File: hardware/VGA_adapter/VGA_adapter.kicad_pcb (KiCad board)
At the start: 2 copper layers, 19.2 x 25.8 mm, 38 parts, among them J1 DF12NB(3.0)-30DS-0.5V(51), J2 DF12NB(3.0)-30DS-0.5V(51), J3 FPC Cable connector 1x15, U1 TXS0102DQMR

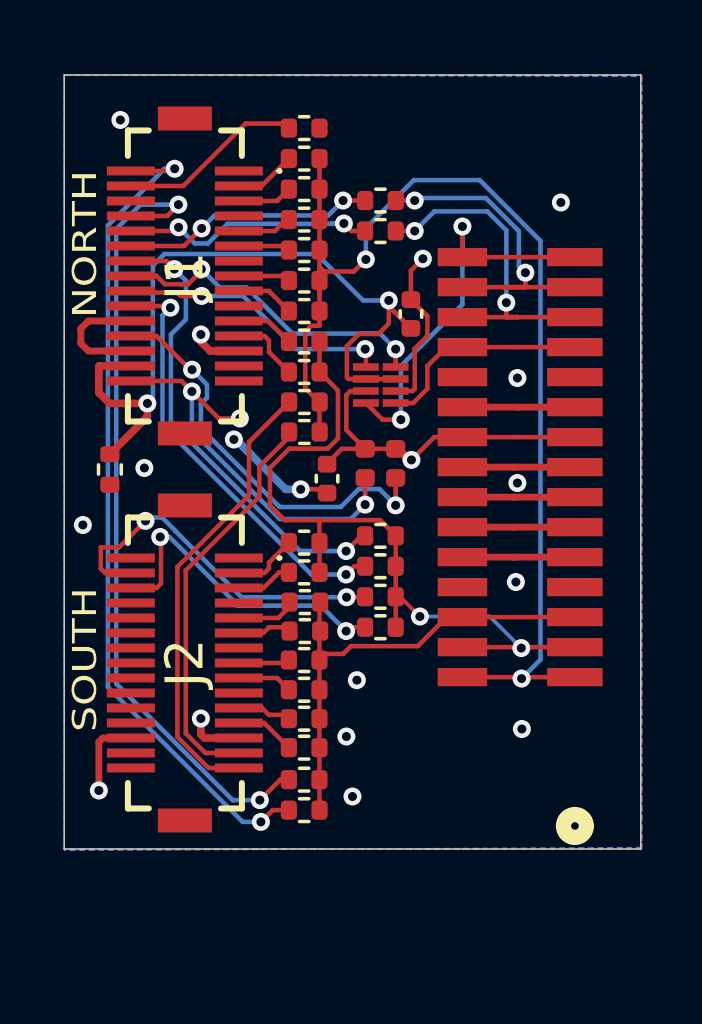
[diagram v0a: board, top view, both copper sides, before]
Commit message: Fix transitors (correct is NMOS, fast version selected). Added charge pump. Fixed level translator pinout.
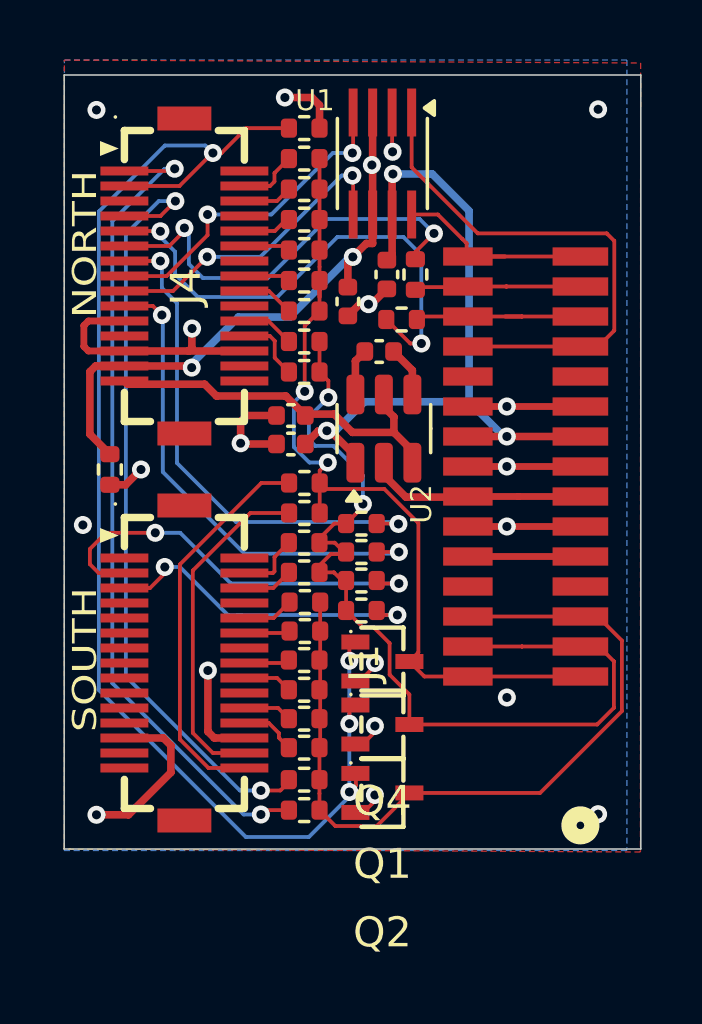
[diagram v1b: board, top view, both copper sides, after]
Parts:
- removed D1, D2: NSR05F40NXT5G, Diode_SMD:D_0402_1005Metric
- removed J2: DF12NB(3.0)-30DS-0.5V(51), Library:DF12NB3030DP05V51
- added C3: 2.2uF, Capacitor_SMD:C_0402_1005Metric, F.Cu at (153.8, 93.0)
- added C4: 2.2uF, Capacitor_SMD:C_0402_1005Metric, F.Cu at (153.8, 92.1)
- added C5: 2.2uF, Capacitor_SMD:C_0402_1005Metric, F.Cu at (156.7, 90.0)
- added J4: DF12NB(3.0)-30DS-0.5V(51), easyeda2kicad:CONN-SMD_30P-P0.50_HRS_DF12NB-3.0-30DP-0.5V, F.Cu at (150.2, 87.4)
- added Q1: NX3008NBKW,115, easyeda2kicad:SOT-323-3_L2.0-W1.3-P1.30-LS2.1-BR, F.Cu at (156.8, 102.4)
- added Q2: NX3008NBKW,115, easyeda2kicad:SOT-323-3_L2.0-W1.3-P1.30-LS2.1-BR, F.Cu at (156.8, 104.7)
- added Q4: NX3008NBKW,115, easyeda2kicad:SOT-323-3_L2.0-W1.3-P1.30-LS2.1-BR, F.Cu at (156.8, 100.3)
- added U2: HE9009M6R, Package_TO_SOT_SMD:SOT-23-6, F.Cu at (156.9, 92.5)
- C1, C2: value 0.1uF -> 2.2uF; footprint Library:C_0402_1005Metric -> Capacitor_SMD:C_0402_1005Metric
- J1: footprint Library:DF12NB3030DP05V51 -> easyeda2kicad:CONN-SMD_30P-P0.50_HRS_DF12NB-3.0-30DP-0.5V
- U1: value TXS0102DQMR -> TXS0102DCT; footprint Library:DQM8 -> Package_SO:SSOP-8_2.95x2.8mm_P0.65mm
- moved J1 12.9 mm to (150.2, 100.3), turned to -90 degrees
- moved G*** 10.5 mm to (152.5, 96.8)
- moved U1 7.38 mm to (156.8, 83.7), turned to -90 degrees
- moved C2 5.95 mm to (155.7, 88.3)
- moved G*** 4.00 mm to (150.0, 82.6), turned to 0 degrees
- moved R27 3.03 mm to (157.5, 88.9)
- moved R28 2.73 mm to (157.9, 87.4), turned to -90 degrees
- moved R8 2.70 mm to (154.2, 94.3)
- moved R9 2.70 mm to (154.2, 95.3)
- moved C1 1.54 mm to (157.0, 87.4), turned to -90 degrees
- moved R12 0.85 mm to (156.2, 98.6), turned to 0 degrees
- moved R13 0.83 mm to (156.2, 97.6), turned to 0 degrees
- moved R17 0.79 mm to (156.2, 96.7), turned to 0 degrees
- moved R16 0.75 mm to (156.2, 95.7), turned to 0 degrees
- moved J3 0.18 mm to (163.4, 100.8)
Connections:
- C1 pad 1: VCC3V3 -> V_VGA
- C2 pad 1: V_VGA -> VCC3V3
- J1 pad 10: Net-(J1-9) -> B6
- J1 pad 11: R5 -> unconnected-(J1-12-Pad11)
- J1 pad 12: Net-(J1-11) -> B7
- J1 pad 14: G1 -> unconnected-(J1-13-Pad14)
- J1 pad 15: R2 -> unconnected-(J1-16-Pad15)
- J1 pad 16: SDA -> B4
- J1 pad 17: R3 -> unconnected-(J1-18-Pad17)
- J1 pad 18: SCK -> B5
- J1 pad 2: B1 -> unconnected-(J1-1-Pad2)
- J1 pad 20: G0 -> unconnected-(J1-19-Pad20)
- J1 pad 21: G6 -> unconnected-(J1-22-Pad21)
- J1 pad 22: GND -> B2
- J1 pad 23: G7 -> unconnected-(J1-24-Pad23)
- J1 pad 24: VCCIN -> B3
- J1 pad 28: VCC3V3 -> R0
- J1 pad 3: R6 -> G4
- J1 pad 30: +3V3 -> R1
- J1 pad 4: LCD_DE -> G2
- J1 pad 5: R7 -> G5
- J1 pad 6: unconnected-(J1-5-Pad6) -> G3
- J1 pad 8: B0 -> unconnected-(J1-7-Pad8)
- J1 pad 9: R4 -> unconnected-(J1-10-Pad9)
- R27 pad 1: Net-(J1-9) -> /HSYNC_IN
- R28 pad 1: Net-(J1-11) -> /VSYNC_IN
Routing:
- net LCD_DE: track 6.19 -> 44.6 mm, vias 0 -> 4
- net /HSYNC_IN: track 0.00 -> 16.9 mm, vias 0 -> 2
- net /VSYNC_IN: track 0.00 -> 14.1 mm, vias 0 -> 2
- net VCCIN: track 13.9 -> 0.00 mm, vias 2 -> 0
- net V_VGA: track 12.5 -> 25.3 mm, vias 1 -> 3
- net GND: track 39.7 -> 51.7 mm, vias 17 -> 19
- net RED: track 39.8 -> 28.4 mm
- net BLUE: track 16.3 -> 26.9 mm
- net SDA_SHIFTED: track 7.19 -> 17.7 mm
- net Net-(J1-9): track 8.46 -> 0.00 mm, vias 2 -> 0
- net Net-(J1-11): track 8.44 -> 0.00 mm, vias 2 -> 0
- net GREEN: track 26.4 -> 32.4 mm
- net VCC3V3: track 25.9 -> 20.0 mm, vias 2 -> 3
- net SCK_SHIFTED: track 13.5 -> 7.70 mm, vias 2 -> 0
- net LCD_VSYNC: track 11.1 -> 5.49 mm, vias 2 -> 0
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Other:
- board text added: "VERSION:"
- board text added: "VGA adapter v0.11"
- board text removed: "+"
- board text removed: "-"
- board text removed: "CERN OHL-S license"
- board text removed: "VGA Adapter V0.09"

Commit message: fixed mixup of pins G5/G4 (3rd diff pair ODD) and DE/PCLK (3rd diff pair EVEN), now with correct polarity for diff pairs
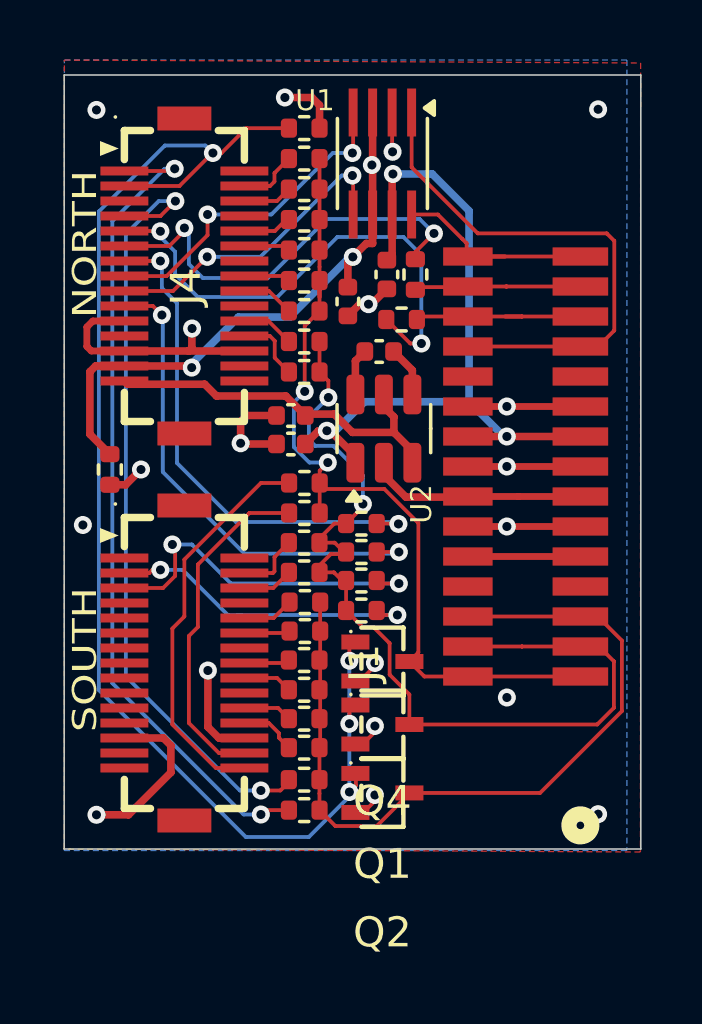
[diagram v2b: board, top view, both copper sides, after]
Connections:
- J1 pad 3: G4 -> G5
- J1 pad 5: G5 -> G4
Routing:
- net G4: track 14.0 -> 11.8 mm

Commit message: review and update manufacturing constraints (via size, etc.)
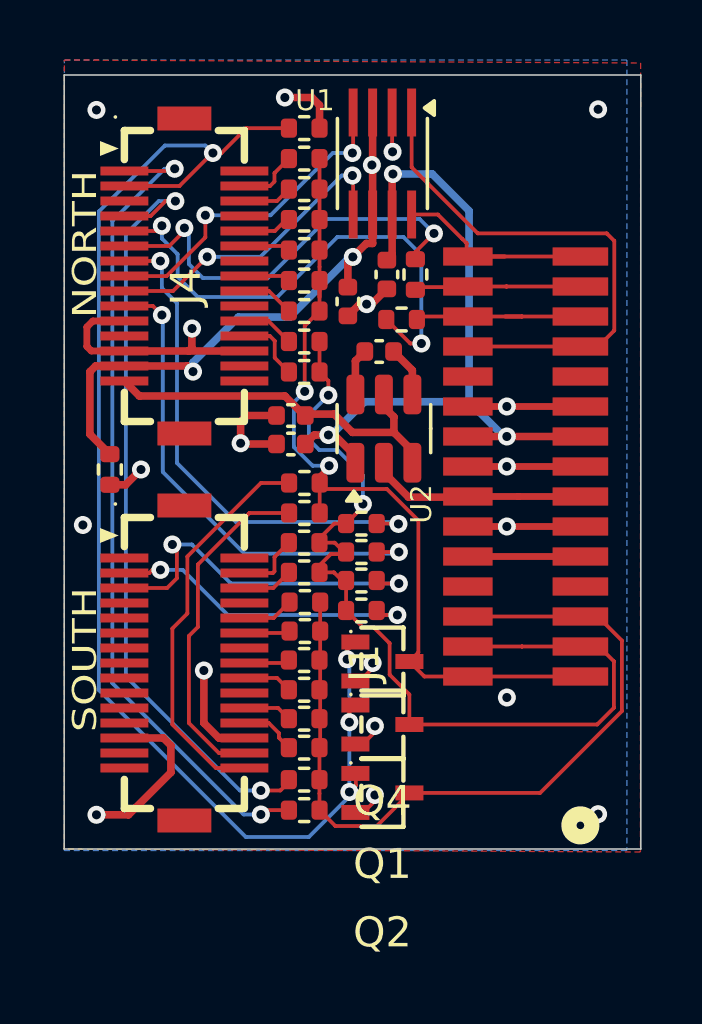
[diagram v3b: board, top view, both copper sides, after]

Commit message: correct footprint of VGA adapter's level translator
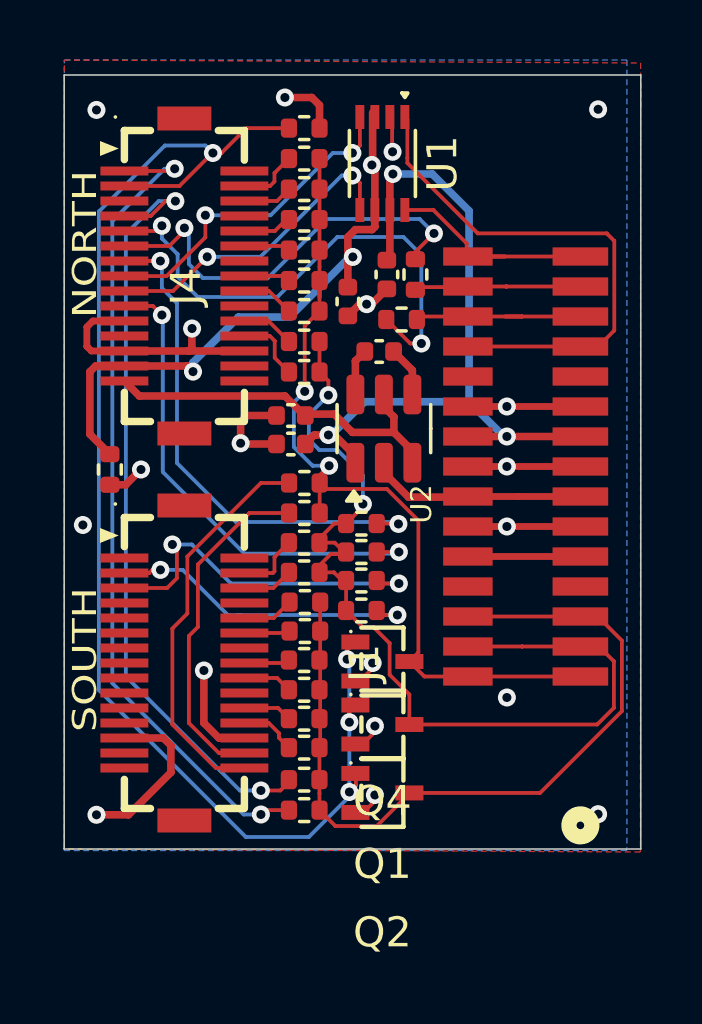
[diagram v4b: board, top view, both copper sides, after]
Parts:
- U1: value TXS0102DCT -> TXS0102DCU; footprint Package_SO:SSOP-8_2.95x2.8mm_P0.65mm -> Package_SO:VSSOP-8_2.3x2mm_P0.5mm
